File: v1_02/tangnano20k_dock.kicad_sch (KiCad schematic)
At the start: 49 parts, among them J1 Mini-DIN-6, J12 Cliff DC10A, J14 Mini-DIN-6, J18 Conn_02x04_Odd_Even, J2 2x20 Pin Female, J3 Conn_01x03_Male, J4 Conn_01x20, J5 Conn_01x02, J6 RCA, J7 FCR684205T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

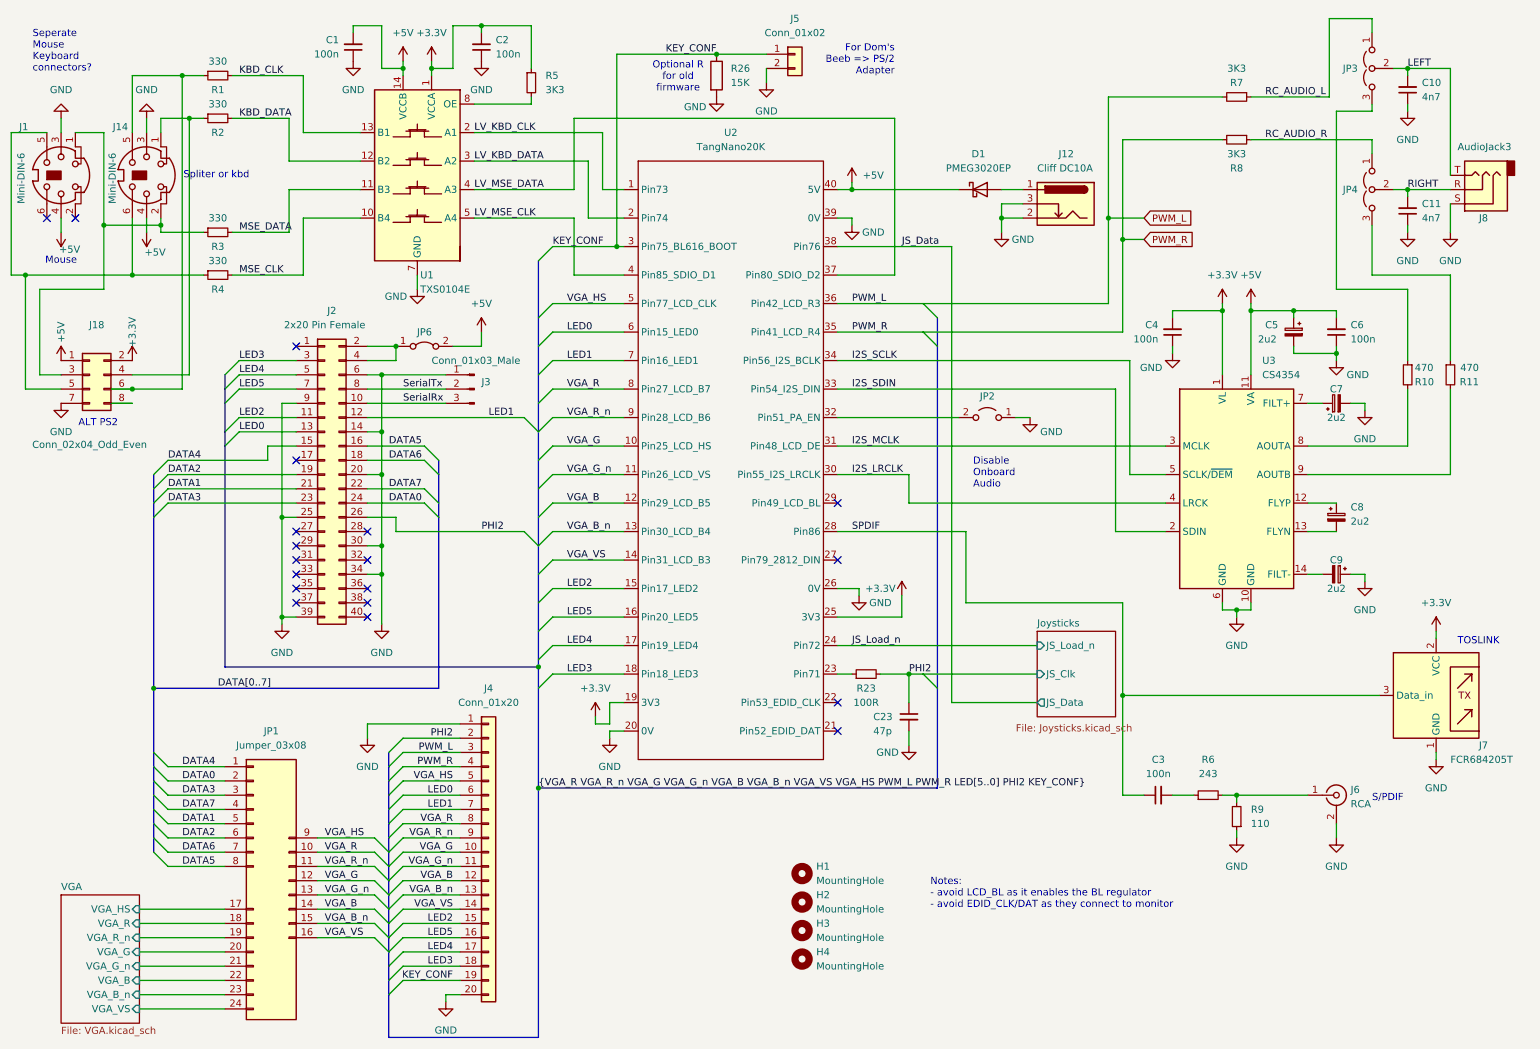
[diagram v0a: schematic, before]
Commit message: v1_02: Fix some ERC warnings
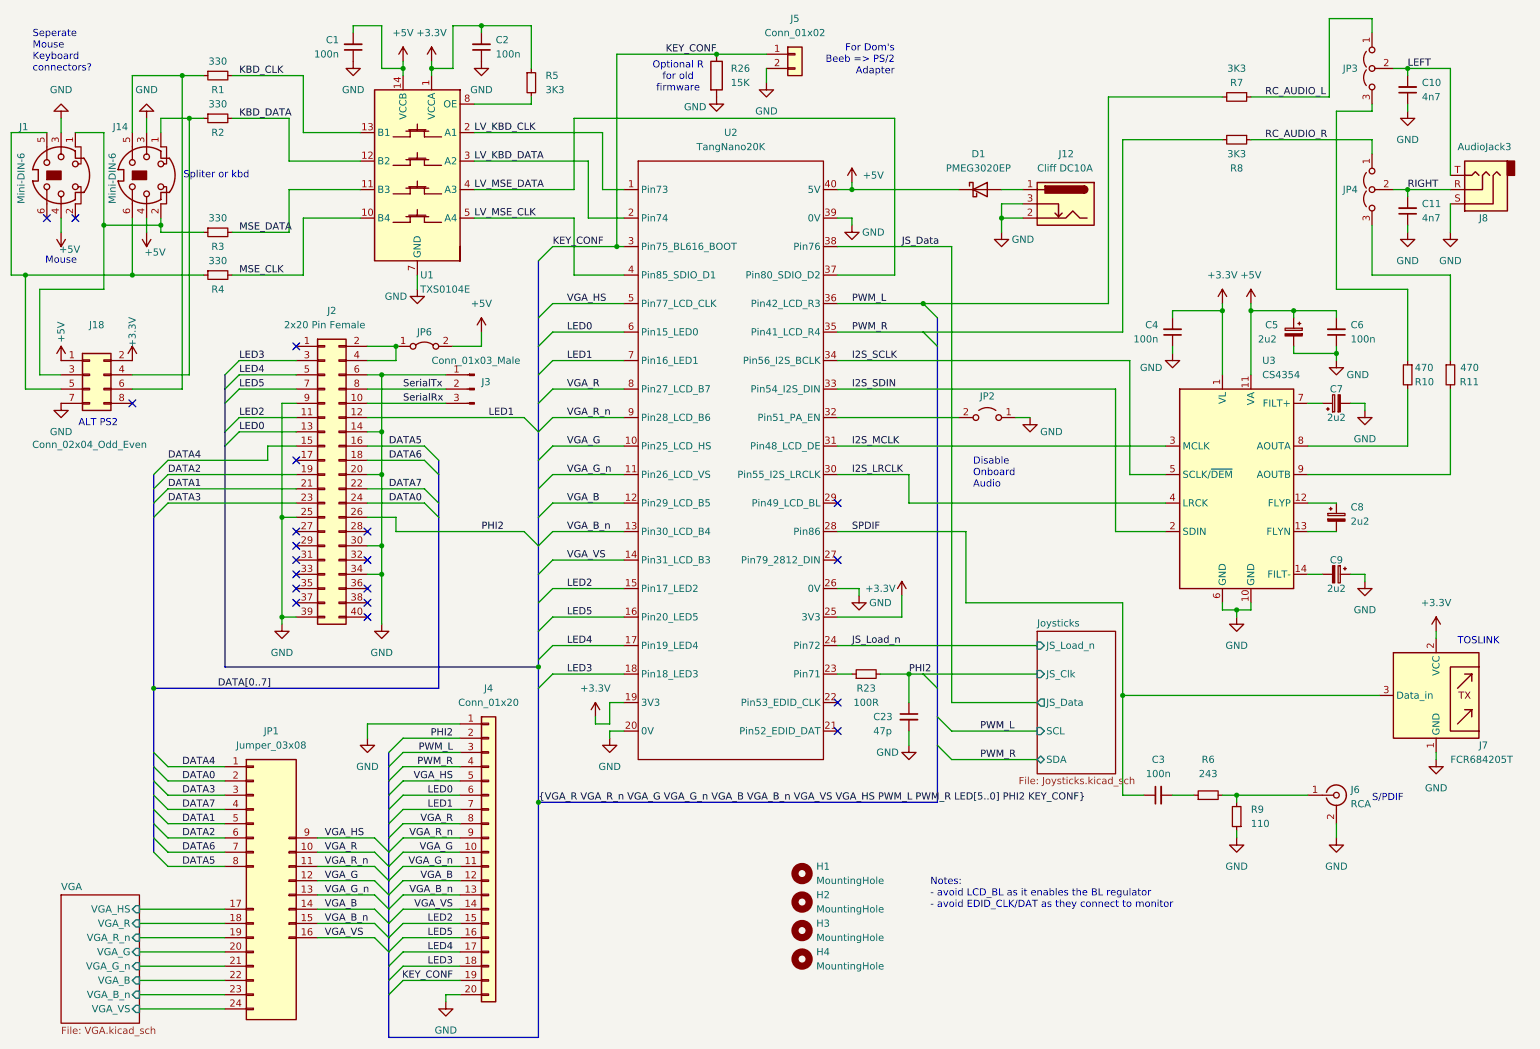
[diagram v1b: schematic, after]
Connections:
- no-connect marks 19 -> 20
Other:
- sheet Joysticks ports: added SCL, SDA; removed none
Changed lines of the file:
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@@
 	)
 	(junction
-		(at 209.55 49.53)
-		(diameter 0)
-		(color 0 0 0 0)
-	)
-	(junction
 		(at 80.01 77.47)
 		(diameter 0)
@@
 	)
 	(junction
-		(at 212.09 53.34)
-		(diameter 0)
-		(color 0 0 0 0)
-	)
-	(junction
 		(at 88.9 22.86)
 		(diameter 0)
@@
 	)
 	(junction
-		(at 35.56 80.01)
-		(diameter 0)
-		(color 0 0 0 0)
-	)
-	(junction
 		(at 40.64 50.8)
 		(diameter 0)
@@
 	)
 	(junction
-		(at 107.95 151.13)
+		(at 176.53 64.77)
 		(diameter 0)
 		(color 0 0 0 0)
@@
 	)
 	(junction
+		(at 107.95 153.67)
+		(diameter 0)
+		(color 0 0 0 0)
+	)
+	(junction
 		(at 16.51 59.69)
 		(diameter 0)
@@
 	)
 	(no_connect
+		(at 35.56 82.55)
+	)
+	(no_connect
 		(at 77.47 105.41)
 	)
@@
 	)
 	(bus_entry
+		(at 179.07 138.43)
+		(size 2.54 2.54)
+		(stroke
+			(width 0)
+			(type default)
+		)
+	)
+	(bus_entry
 		(at 41.91 95.25)
 		(size -2.54 2.54)
@@
 	)
 	(bus_entry
+		(at 179.07 143.51)
+		(size 2.54 2.54)
+		(stroke
+			(width 0)
+			(type default)
+		)
+	)
+	(bus_entry
 		(at 54.61 80.01)
 		(size -2.54 2.54)
@@
 	(wire
 		(pts
+			(xy 181.61 140.97) (xy 196.85 140.97)
+		)
+		(stroke
+			(width 0)
+			(type default)
+		)
+	)
+	(wire
+		(pts
 			(xy 234.95 66.04) (xy 234.95 77.47)
 		)
@@
 	(bus
 		(pts
-			(xy 107.95 151.13) (xy 179.07 151.13)
+			(xy 107.95 153.67) (xy 179.07 153.67)
 		)
 		(stroke
@@
 		)
 	)
+	(bus
+		(pts
+			(xy 107.95 153.67) (xy 107.95 195.58)
+		)
+		(stroke
+			(width 0)
+			(type default)
+		)
+	)
 	(wire
 		(pts
@@
 	(wire
 		(pts
-			(xy 35.56 82.55) (xy 31.75 82.55)
-		)
-		(stroke
-			(width 0)
-			(type default)
-		)
-	)
-	(wire
-		(pts
 			(xy 77.47 139.7) (xy 93.98 139.7)
 		)
@@
 	(wire
 		(pts
-			(xy 212.09 53.34) (xy 215.9 53.34)
-		)
-		(stroke
-			(width 0)
-			(type default)
-		)
-	)
-	(wire
-		(pts
 			(xy 22.86 52.07) (xy 22.86 49.53)
 		)
@@
 	(wire
 		(pts
-			(xy 209.55 49.53) (xy 209.55 27.94)
+			(xy 209.55 27.94) (xy 209.55 64.77)
 		)
 		(stroke
@@
 		)
 	)
-	(wire
-		(pts
-			(xy 209.55 64.77) (xy 209.55 49.53)
-		)
-		(stroke
-			(width 0)
-			(type default)
-		)
-	)
 	(bus
 		(pts
@@
 	(wire
 		(pts
-			(xy 209.55 49.53) (xy 215.9 49.53)
-		)
-		(stroke
-			(width 0)
-			(type default)
-		)
-	)
-	(wire
-		(pts
 			(xy 114.3 49.53) (xy 114.3 59.69)
 		)
@@
 	(bus
 		(pts
-			(xy 179.07 133.35) (xy 179.07 151.13)
+			(xy 179.07 133.35) (xy 179.07 138.43)
 		)
 		(stroke
@@
 		)
 	)
-	(wire
-		(pts
-			(xy 212.09 69.85) (xy 212.09 53.34)
-		)
-		(stroke
-			(width 0)
-			(type default)
-		)
-	)
 	(bus
 		(pts
@@
 	(bus
 		(pts
-			(xy 107.95 151.13) (xy 107.95 195.58)
+			(xy 107.95 133.35) (xy 107.95 153.67)
 		)
 		(stroke
@@
 		)
 	)
-	(bus
-		(pts
-			(xy 107.95 133.35) (xy 107.95 151.13)
-		)
-		(stroke
-			(width 0)
-			(type default)
-		)
-	)
 	(wire
 		(pts
@@
 		)
 	)
+	(bus
+		(pts
+			(xy 179.07 138.43) (xy 179.07 143.51)
+		)
+		(stroke
+			(width 0)
+			(type default)
+		)
+	)
+	(bus
+		(pts
+			(xy 179.07 143.51) (xy 179.07 153.67)
+		)
+		(stroke
+			(width 0)
+			(type default)
+		)
+	)
 	(wire
 		(pts
@@
 	(wire
 		(pts
-			(xy 212.09 53.34) (xy 212.09 35.56)
+			(xy 212.09 35.56) (xy 212.09 69.85)
 		)
 		(stroke
@@
 	(wire
 		(pts
-			(xy 35.56 80.01) (xy 31.75 80.01)
-		)
-		(stroke
-			(width 0)
-			(type default)
-		)
-	)
-	(wire
-		(pts
 			(xy 68.58 162.56) (xy 78.74 162.56)
 		)
@@
 	(wire
 		(pts
+			(xy 181.61 146.05) (xy 196.85 146.05)
+		)
+		(stroke
+			(width 0)
+			(type default)
+		)
+	)
+	(wire
+		(pts
 			(xy 53.34 31.75) (xy 63.5 31.75)
 		)
@@
 	)
 	(image
-		(at 132.08 173.99)
+		(at 132.08 176.53)
 		(data "iVBORw0KGgoAAAANSUhEUgAAAPYAAAHWCAIAAADLq+MdAAAAA3NCSVQICAjb4U/gAAAgAElEQVR4"
 			"nOy9d5xdVdU+/jxrn3PvlMykQXohhACh91BFEJAqgnRFRRQVyyvYsCMiqPhaUPTF9+uLggr6U0QE"
@@
 		)
 	)
+	(label "PWM_R"
+		(at 186.69 146.05 0)
+		(effects
+			(font
+				(size 1.27 1.27)
+			)
+			(justify left bottom)
+		)
+	)
 	(label "{VGA_R VGA_R_n VGA_G VGA_G_n VGA_B VGA_B_n VGA_VS VGA_HS PWM_L PWM_R LED[5..0] PHI2 KEY_CONF}"
-		(at 107.95 151.13 0)
+		(at 107.95 153.67 0)
 		(effects
 			(font
@@
 		)
 	)
+	(label "PWM_L"
+		(at 186.69 140.97 0)
+		(effects
+			(font
+				(size 1.27 1.27)
+			)
+			(justify left bottom)
+		)
+	)
 	(label "DATA5"
 		(at 81.28 90.17 0)
@@
 		)
 	)
-	(global_label "PWM_L"
-		(shape input)
-		(at 215.9 49.53 0)
-		(fields_autoplaced yes)
-		(effects
-			(font
-				(size 1.27 1.27)
-			)
-			(justify left)
-		)
-		(property "Intersheetrefs" "${INTERSHEET_REFS}"
-			(at 225.0537 49.53 0)
-			(effects
-				(font
-					(size 1.27 1.27)
-				)
-				(justify left)
-				(hide yes)
-			)
-		)
-	)
-	(global_label "PWM_R"
-		(shape input)
-		(at 215.9 53.34 0)
-		(fields_autoplaced yes)
-		(effects
-			(font
-				(size 1.27 1.27)
-			)
-			(justify left)
-		)
-		(property "Intersheetrefs" "${INTERSHEET_REFS}"
-			(at 225.2956 53.34 0)
-			(effects
-				(font
-					(size 1.27 1.27)
-				)
-				(justify left)
-				(hide yes)
-			)
-		)
-	)
 	(symbol
 		(lib_id "Device:R_Small")
@@
 	(sheet
 		(at 196.85 123.19)
-		(size 13.97 15.24)
+		(size 13.97 25.4)
 		(exclude_from_sim no)
 		(in_bom yes)
@@
 		)
 		(property "Sheetfile" "Joysticks.kicad_sch"
-			(at 193.04 139.7 0)
+			(at 193.548 149.098 0)
 			(effects
 				(font
@@
 			(effects
 				(font
+					(size 1.27 1.27)
+				)
+				(justify left)
+			)
+		)
+		(pin "SCL" input
+			(at 196.85 140.97 180)
+			(effects
+				(font
+					(size 1.27 1.27)
+				)
+				(justify left)
+			)
+		)
+		(pin "SDA" bidirectional
+			(at 196.85 146.05 180)
+			(effects
+				(font
